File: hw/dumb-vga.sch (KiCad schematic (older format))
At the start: 20 parts, among them IC1 74HC590N, IC2 74HC590N, IC3 74HC590N, IC4 74HC574N, IC5 74HC574N, U1 A29040C, X1 VGAF

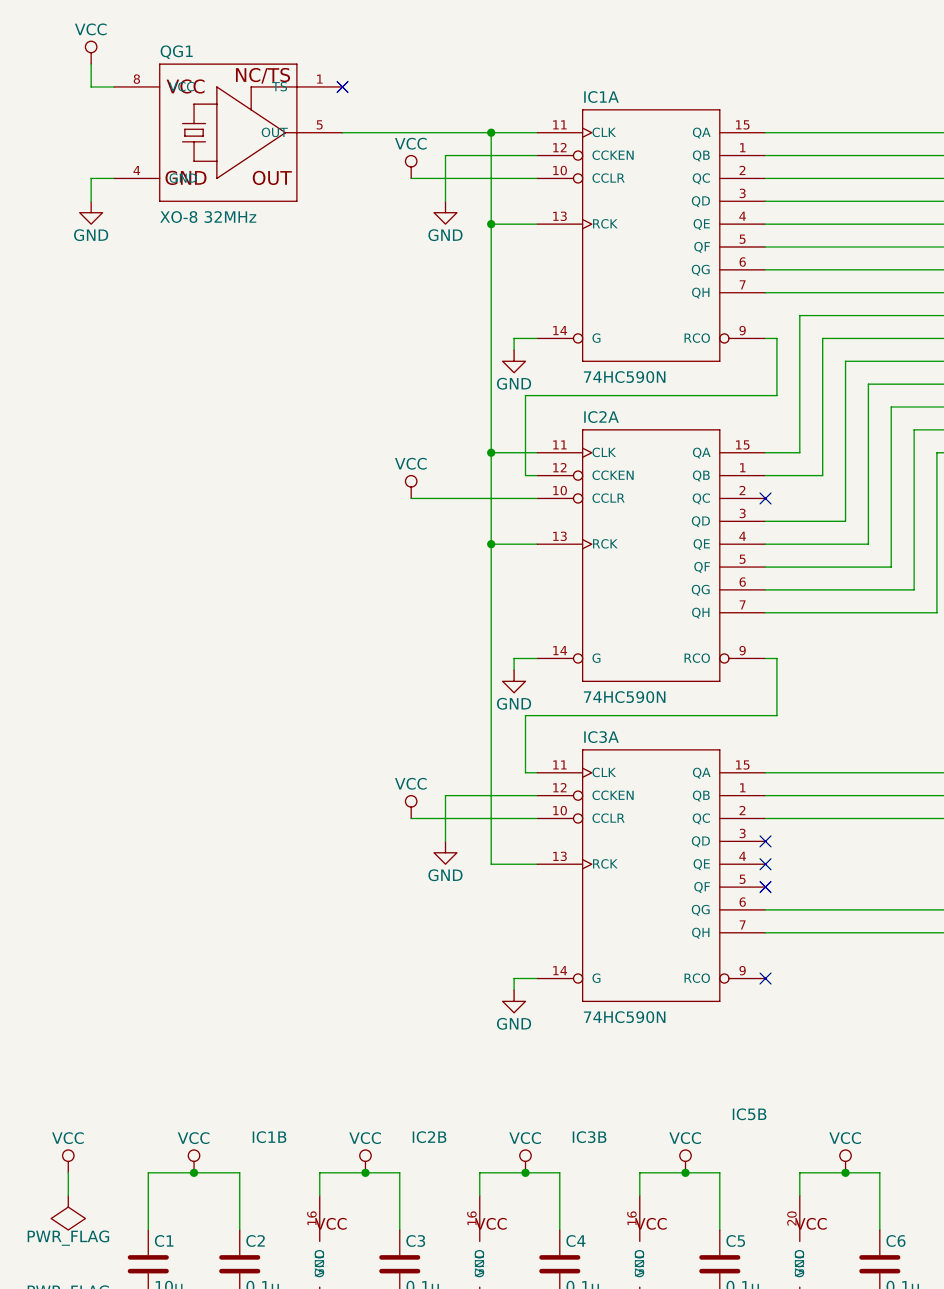
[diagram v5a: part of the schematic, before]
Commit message: Add scan-line doubling
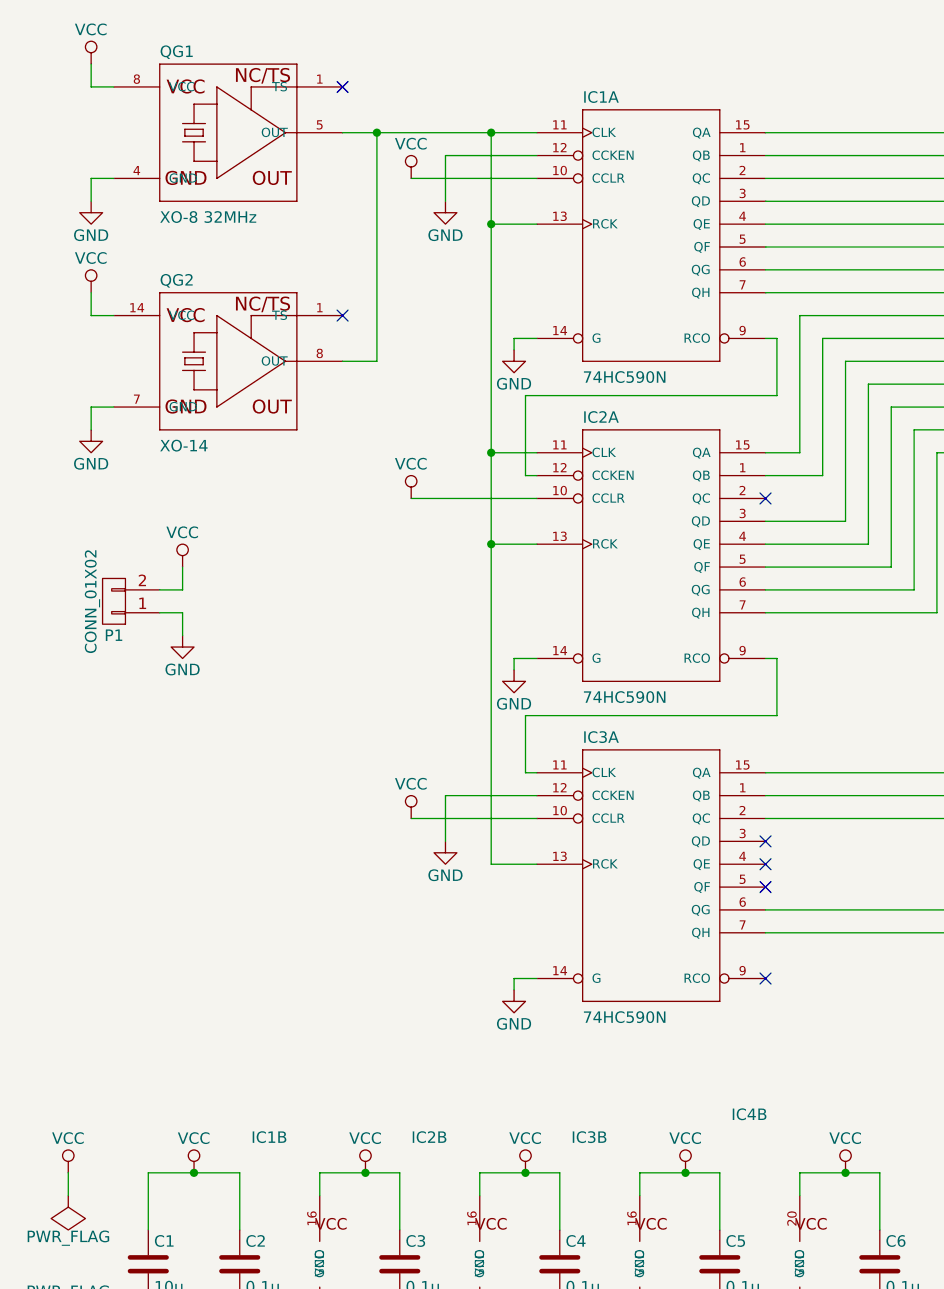
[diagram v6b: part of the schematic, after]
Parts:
- added P1: CONN_01X02, Pin_Headers:Pin_Header_Angled_1x02, symbol CONN_01X02
- added QG2: XO-14, Housings_DIP:DIP-14_W7.62mm, symbol XO-14
- C1, C2, C3, C4, C5, C6: footprint (none) -> Capacitors_ThroughHole:C_Rect_L7_W2.5_P5
- IC1, IC2, IC3: footprint 74xx-eu-DIL16 -> Housings_DIP:DIP-16_W7.62mm
- IC4: footprint 74xx-eu-DIL20 -> Housings_DIP:DIP-20_W7.62mm
- IC4: renamed from IC5; footprint 74xx-eu-DIL20 -> Housings_DIP:DIP-20_W7.62mm
- QG1: footprint crystal-DIL08S -> Housings_DIP:DIP-8_W7.62mm
- R1, R2, R3, R4, R5, R6: footprint (none) -> Resistors_ThroughHole:Resistor_Horizontal_RM10mm
- U1: footprint (none) -> Housings_DIP:DIP-32_W15.24mm
- X1: footprint HD15_B-HD15F -> HD15_B:HD15_B-HD15F
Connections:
- net GND: now also P1.1 (P1), QG2.7 (GND)
- net VCC: now also P1.2 (P2), QG2.14 (VCC)
- net at IC1.11 (CLK), IC1.13 (RCK), IC2.11 (CLK)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: now also QG2.8 (OUT)
- no-connect marks 13 -> 14
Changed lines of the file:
@@
 Title "Dumb VGA"
 Date ""
-Rev "v0.4"
+Rev "v0.5"
 Comp ""
 Comment1 "Simple circuit to generate VGA-like signal"
@@
 F 0 "IC1" H 3100 2325 50  0000 L BNN
 F 1 "74HC590N" H 3100 1100 50  0000 L BNN
-F 2 "74xx-eu-DIL16" H 3400 1950 50  0001 C CNN
+F 2 "Housings_DIP:DIP-16_W7.62mm" H 3400 1950 50  0001 C CNN
 F 3 "" H 3400 1800 60  0000 C CNN
 	1    3400 1800
@@
 F 0 "IC1" H 1650 6875 50  0000 L BNN
 F 1 "74HC590N" H 1650 5650 50  0000 L BNN
-F 2 "74xx-eu-DIL16" H 1950 6500 50  0001 C CNN
+F 2 "Housings_DIP:DIP-16_W7.62mm" H 1950 6500 50  0001 C CNN
 F 3 "" H 1950 6350 60  0000 C CNN
 	2    1950 6350
@@
 F 0 "IC2" H 2350 6875 50  0000 L BNN
 F 1 "74HC590N" H 2350 5650 50  0000 L BNN
-F 2 "74xx-eu-DIL16" H 2650 6500 50  0001 C CNN
+F 2 "Housings_DIP:DIP-16_W7.62mm" H 2650 6500 50  0001 C CNN
 F 3 "" H 2650 6350 60  0000 C CNN
 	2    2650 6350
@@
 F 0 "IC3" H 3050 6875 50  0000 L BNN
 F 1 "74HC590N" H 3050 5650 50  0000 L BNN
-F 2 "74xx-eu-DIL16" H 3350 6500 50  0001 C CNN
+F 2 "Housings_DIP:DIP-16_W7.62mm" H 3350 6500 50  0001 C CNN
 F 3 "" H 3350 6350 60  0000 C CNN
 	2    3350 6350
@@
 F 0 "IC3" H 3100 5125 50  0000 L BNN
 F 1 "74HC590N" H 3100 3900 50  0000 L BNN
-F 2 "74xx-eu-DIL16" H 3400 4750 50  0001 C CNN
+F 2 "Housings_DIP:DIP-16_W7.62mm" H 3400 4750 50  0001 C CNN
 F 3 "" H 3400 4600 60  0000 C CNN
 	1    3400 4600
@@
 F 0 "C3" H 2325 6450 50  0000 L CNN
 F 1 "0.1u" H 2325 6250 50  0000 L CNN
-F 2 "" H 2338 6200 50  0000 C CNN
+F 2 "Capacitors_ThroughHole:C_Rect_L7_W2.5_P5" H 2338 6200 50  0001 C CNN
 F 3 "" H 2300 6350 50  0000 C CNN
 	1    2300 6350
@@
 F 0 "C4" H 3025 6450 50  0000 L CNN
 F 1 "0.1u" H 3025 6250 50  0000 L CNN
-F 2 "" H 3038 6200 50  0000 C CNN
+F 2 "Capacitors_ThroughHole:C_Rect_L7_W2.5_P5" H 3038 6200 50  0001 C CNN
 F 3 "" H 3000 6350 50  0000 C CNN
 	1    3000 6350
@@
 F 0 "C5" H 3725 6450 50  0000 L CNN
 F 1 "0.1u" H 3725 6250 50  0000 L CNN
-F 2 "" H 3738 6200 50  0000 C CNN
+F 2 "Capacitors_ThroughHole:C_Rect_L7_W2.5_P5" H 3738 6200 50  0001 C CNN
 F 3 "" H 3700 6350 50  0000 C CNN
 	1    3700 6350
@@
 F 0 "C2" H 1625 6450 50  0000 L CNN
 F 1 "0.1u" H 1625 6250 50  0000 L CNN
-F 2 "" H 1638 6200 50  0000 C CNN
+F 2 "Capacitors_ThroughHole:C_Rect_L7_W2.5_P5" H 1638 6200 50  0001 C CNN
 F 3 "" H 1600 6350 50  0000 C CNN
 	1    1600 6350
@@
 F 0 "C1" H 1225 6450 50  0000 L CNN
 F 1 "10u" H 1225 6250 50  0000 L CNN
-F 2 "" H 1238 6200 50  0000 C CNN
+F 2 "Capacitors_ThroughHole:C_Rect_L7_W2.5_P5" H 1238 6200 50  0001 C CNN
 F 3 "" H 1200 6350 50  0000 C CNN
 	1    1200 6350
@@
 F 0 "QG1" H 1250 1725 50  0000 L BNN
 F 1 "XO-8 32MHz" H 1250 1000 50  0000 L BNN
-F 2 "crystal-DIL08S" H 1550 1550 50  0001 C CNN
+F 2 "Housings_DIP:DIP-8_W7.62mm" H 1550 1550 50  0001 C CNN
 F 3 "" H 1550 1400 60  0000 C CNN
 	1    1550 1400
@@
 F 0 "R4" V 9130 1550 50  0000 C CNN
 F 1 "680" V 9050 1550 50  0000 C CNN
-F 2 "" V 8980 1550 50  0000 C CNN
+F 2 "Resistors_ThroughHole:Resistor_Horizontal_RM10mm" V 8980 1550 50  0001 C CNN
 F 3 "" H 9050 1550 50  0000 C CNN
 	1    9050 1550
@@
 F 0 "R5" V 9130 1800 50  0000 C CNN
 F 1 "680" V 9050 1800 50  0000 C CNN
-F 2 "" V 8980 1800 50  0000 C CNN
+F 2 "Resistors_ThroughHole:Resistor_Horizontal_RM10mm" V 8980 1800 50  0001 C CNN
 F 3 "" H 9050 1800 50  0000 C CNN
 	1    9050 1800
@@
 F 0 "R6" V 9130 2050 50  0000 C CNN
 F 1 "680" V 9050 2050 50  0000 C CNN
-F 2 "" V 8980 2050 50  0000 C CNN
+F 2 "Resistors_ThroughHole:Resistor_Horizontal_RM10mm" V 8980 2050 50  0001 C CNN
 F 3 "" H 9050 2050 50  0000 C CNN
 	1    9050 2050
@@
 F 0 "R1" V 8880 1450 50  0000 C CNN
 F 1 "1.5K" V 8800 1450 50  0000 C CNN
-F 2 "" V 8730 1450 50  0000 C CNN
+F 2 "Resistors_ThroughHole:Resistor_Horizontal_RM10mm" V 8730 1450 50  0001 C CNN
 F 3 "" H 8800 1450 50  0000 C CNN
 	1    8800 1450
@@
 F 0 "R2" V 8880 1700 50  0000 C CNN
 F 1 "1.5K" V 8800 1700 50  0000 C CNN
-F 2 "" V 8730 1700 50  0000 C CNN
+F 2 "Resistors_ThroughHole:Resistor_Horizontal_RM10mm" V 8730 1700 50  0001 C CNN
 F 3 "" H 8800 1700 50  0000 C CNN
 	1    8800 1700
@@
 F 0 "R3" V 8880 1950 50  0000 C CNN
 F 1 "1.5K" V 8800 1950 50  0000 C CNN
-F 2 "" V 8730 1950 50  0000 C CNN
+F 2 "Resistors_ThroughHole:Resistor_Horizontal_RM10mm" V 8730 1950 50  0001 C CNN
 F 3 "" H 8800 1950 50  0000 C CNN
 	1    8800 1950
@@
 F 0 "X1" H 10000 2390 50  0000 L BNN
 F 1 "VGAF" H 10070 1140 50  0000 L BNN
-F 2 "HD15_B-HD15F" H 9800 2000 50  0001 C CNN
+F 2 "HD15_B:HD15_B-HD15F" H 9800 2000 50  0001 C CNN
 F 3 "" H 9800 1850 60  0000 C CNN
 	1    9800 1850
@@
 F 0 "U1" H 5900 3400 50  0000 C CNN
 F 1 "A29040C" H 6100 1000 50  0000 C CNN
-F 2 "" H 6100 2400 50  0000 C CNN
+F 2 "Housings_DIP:DIP-32_W15.24mm" H 6100 2400 50  0001 C CNN
 F 3 "" H 6100 2400 50  0000 C CNN
 	1    6100 2400
@@
 F 0 "IC4" H 7300 2625 50  0000 L BNN
 F 1 "74HC574N" H 7300 1300 50  0000 L BNN
-F 2 "74xx-eu-DIL20" H 7600 2150 50  0001 C CNN
+F 2 "Housings_DIP:DIP-20_W7.62mm" H 7600 2150 50  0001 C CNN
 F 3 "" H 7600 2000 60  0000 C CNN
 	1    7600 2000
@@
 	7000 2400 7100 2400
 $Comp
-L 74HC574N IC5
+L 74HC574N IC4
 U 2 1 56DAD254
 P 4050 6350
-F 0 "IC5" H 3750 6975 50  0000 L BNN
+F 0 "IC4" H 3750 6975 50  0000 L BNN
 F 1 "74HC574N" H 3750 5650 50  0000 L BNN
-F 2 "74xx-eu-DIL20" H 4050 6500 50  0001 C CNN
+F 2 "Housings_DIP:DIP-20_W7.62mm" H 4050 6500 50  0001 C CNN
 F 3 "" H 4050 6350 60  0000 C CNN
 	2    4050 6350
@@
 F 0 "C6" H 4425 6450 50  0000 L CNN
 F 1 "0.1u" H 4425 6250 50  0000 L CNN
-F 2 "" H 4438 6200 50  0000 C CNN
+F 2 "Capacitors_ThroughHole:C_Rect_L7_W2.5_P5" H 4438 6200 50  0001 C CNN
 F 3 "" H 4400 6350 50  0000 C CNN
 	1    4400 6350
@@
 F 0 "IC2" H 3100 3725 50  0000 L BNN
 F 1 "74HC590N" H 3100 2500 50  0000 L BNN
-F 2 "74xx-eu-DIL16" H 3400 3350 50  0001 C CNN
+F 2 "Housings_DIP:DIP-16_W7.62mm" H 3400 3350 50  0001 C CNN
 F 3 "" H 3400 3200 60  0000 C CNN
 	1    3400 3200
@@
 Wire Wire Line
 	5050 4800 3900 4800
+$Comp
+L XO-14 QG2
+U 1 1 56E0A684
+P 1550 2400
+F 0 "QG2" H 1250 2725 50  0000 L BNN
+F 1 "XO-14" H 1250 2000 50  0000 L BNN
+F 2 "Housings_DIP:DIP-14_W7.62mm" H 1550 2550 50  0001 C CNN
+F 3 "" H 1550 2400 60  0000 C CNN
+	1    1550 2400
+	1    0    0    -1
+$EndComp
+NoConn ~ 2050 2200
+Wire Wire Line
+	2050 2400 2200 2400
+Wire Wire Line
+	2200 2400 2200 1400
+Connection ~ 2200 1400
+$Comp
+L VCC #PWR029
+U 1 1 56E0A7F2
+P 950 2100
+F 0 "#PWR029" H 950 1950 50  0001 C CNN
+F 1 "VCC" H 950 2250 50  0000 C CNN
+F 2 "" H 950 2100 50  0000 C CNN
+F 3 "" H 950 2100 50  0000 C CNN
+	1    950  2100
+	1    0    0    -1
+$EndComp
+$Comp
+L GND #PWR030
+U 1 1 56E0A845
+P 950 2700
+F 0 "#PWR030" H 950 2450 50  0001 C CNN
+F 1 "GND" H 950 2550 50  0000 C CNN
+F 2 "" H 950 2700 50  0000 C CNN
+F 3 "" H 950 2700 50  0000 C CNN
+	1    950  2700
+	1    0    0    -1
+$EndComp
+Wire Wire Line
+	950  2100 950  2200
+Wire Wire Line
+	950  2200 1050 2200
+Wire Wire Line
+	1050 2600 950  2600
+Wire Wire Line
+	950  2600 950  2700
+$Comp
+L CONN_01X02 P1
+U 1 1 56E0ABB2
+P 1050 3450
+F 0 "P1" H 1050 3600 50  0000 C CNN
+F 1 "CONN_01X02" V 1150 3450 50  0000 C CNN
+F 2 "Pin_Headers:Pin_Header_Angled_1x02" H 1050 3450 50  0001 C CNN
+F 3 "" H 1050 3450 50  0000 C CNN
+	1    1050 3450
+	-1   0    0    1
+$EndComp
+$Comp
+L VCC #PWR031
+U 1 1 56E0AC4F
+P 1350 3300
+F 0 "#PWR031" H 1350 3150 50  0001 C CNN
+F 1 "VCC" H 1350 3450 50  0000 C CNN
+F 2 "" H 1350 3300 50  0000 C CNN
+F 3 "" H 1350 3300 50  0000 C CNN
+	1    1350 3300
+	1    0    0    -1
+$EndComp
+$Comp
+L GND #PWR032
+U 1 1 56E0ACA5
+P 1350 3600
+F 0 "#PWR032" H 1350 3350 50  0001 C CNN
+F 1 "GND" H 1350 3450 50  0000 C CNN
+F 2 "" H 1350 3600 50  0000 C CNN
+F 3 "" H 1350 3600 50  0000 C CNN
+	1    1350 3600
+	1    0    0    -1
+$EndComp
+Wire Wire Line
+	1250 3400 1350 3400
+Wire Wire Line
+	1350 3400 1350 3300
+Wire Wire Line
+	1250 3500 1350 3500
+Wire Wire Line
+	1350 3500 1350 3600
 $EndSCHEMATC
